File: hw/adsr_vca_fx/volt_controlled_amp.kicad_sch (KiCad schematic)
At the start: 34 parts, among them J9 Conn_01x02, U6 LM13700, U6 TL972

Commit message: updated readme
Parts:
- added J11: Conn_01x02, Connector_PinHeader_2.54mm:PinHeader_1x02_P2.54mm_Vertical, symbol Connector_Generic:Conn_01x02
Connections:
- net GND: now also J11.1 (Pin_1)
- net at R14.2, RV7.1, TP1.1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: now also J11.2 (Pin_2)
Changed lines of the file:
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@@
   (junction (at 204.47 95.25) (diameter 0) (color 0 0 0 0)
   )
+  (junction (at 245.11 149.86) (diameter 0) (color 0 0 0 0)
+  )
   (junction (at 241.3 40.64) (diameter 0) (color 0 0 0 0)
   )
@@
     (stroke (width 0) (type default))
   )
+  (wire (pts (xy 260.35 152.4) (xy 260.35 161.29))
+    (stroke (width 0) (type default))
+  )
   (wire (pts (xy 210.82 53.34) (xy 220.98 53.34))
     (stroke (width 0) (type default))
@@
     (stroke (width 0) (type default))
   )
+  (wire (pts (xy 245.11 149.86) (xy 265.43 149.86))
+    (stroke (width 0) (type default))
+  )
   (wire (pts (xy 158.75 257.81) (xy 158.75 260.35))
     (stroke (width 0) (type default))
@@
   )
   (wire (pts (xy 240.03 97.79) (xy 247.65 97.79))
+    (stroke (width 0) (type default))
+  )
+  (wire (pts (xy 265.43 152.4) (xy 260.35 152.4))
     (stroke (width 0) (type default))
   )
@@
     )
   )
+  (symbol (lib_id "Connector_Generic:Conn_01x02") (at 270.51 152.4 0) (mirror x) (unit 1)
+    (in_bom yes) (on_board yes) (dnp no)
+    (property "Reference" "J11" (at 270.51 147.32 0)
+      (effects (font (size 1.27 1.27)))
+    )
+    (property "Value" "Conn_01x02" (at 270.51 147.32 0)
+      (effects (font (size 1.27 1.27)) hide)
+    )
+    (property "Footprint" "Connector_PinHeader_2.54mm:PinHeader_1x02_P2.54mm_Vertical" (at 270.51 152.4 0)
+      (effects (font (size 1.27 1.27)) hide)
+    )
+    (property "Datasheet" "~" (at 270.51 152.4 0)
+      (effects (font (size 1.27 1.27)) hide)
+    )
+    (pin "1")
+    (pin "2")
+    (instances
+      (project "adsr_vca_fx"
+        (path "/2c7cc946-dcca-4ffb-b6a0-bf0c9ddb491b/00108663-9f1e-44dc-8937-64b7d21ff823"
+          (reference "J11") (unit 1)
+        )
+      )
+    )
+  )
   (symbol (lib_id "Device:R_Potentiometer_Trim") (at 226.06 162.56 270) (unit 1)
     (in_bom yes) (on_board yes) (dnp no)
@@
         )
       )
+    )
+  )
+  (symbol (lib_id "power:GND") (at 260.35 161.29 0) (unit 1)
+    (in_bom yes) (on_board yes) (dnp no) (fields_autoplaced)
+    (property "Reference" "#PWR070" (at 260.35 167.64 0)
+      (effects (font (size 1.27 1.27)) hide)
+    )
+    (property "Value" "GND" (at 260.35 166.37 0)
+      (effects (font (size 1.27 1.27)))
+    )
+    (property "Footprint" "" (at 260.35 161.29 0)
+      (effects (font (size 1.27 1.27)) hide)
+    )
+    (property "Datasheet" "" (at 260.35 161.29 0)
+      (effects (font (size 1.27 1.27)) hide)
+    )
+    (pin "1")
+    (instances
+      (project "adsr_vca_fx"
+        (path "/2c7cc946-dcca-4ffb-b6a0-bf0c9ddb491b/00108663-9f1e-44dc-8937-64b7d21ff823"
+          (reference "#PWR070") (unit 1)
+        )
+      )

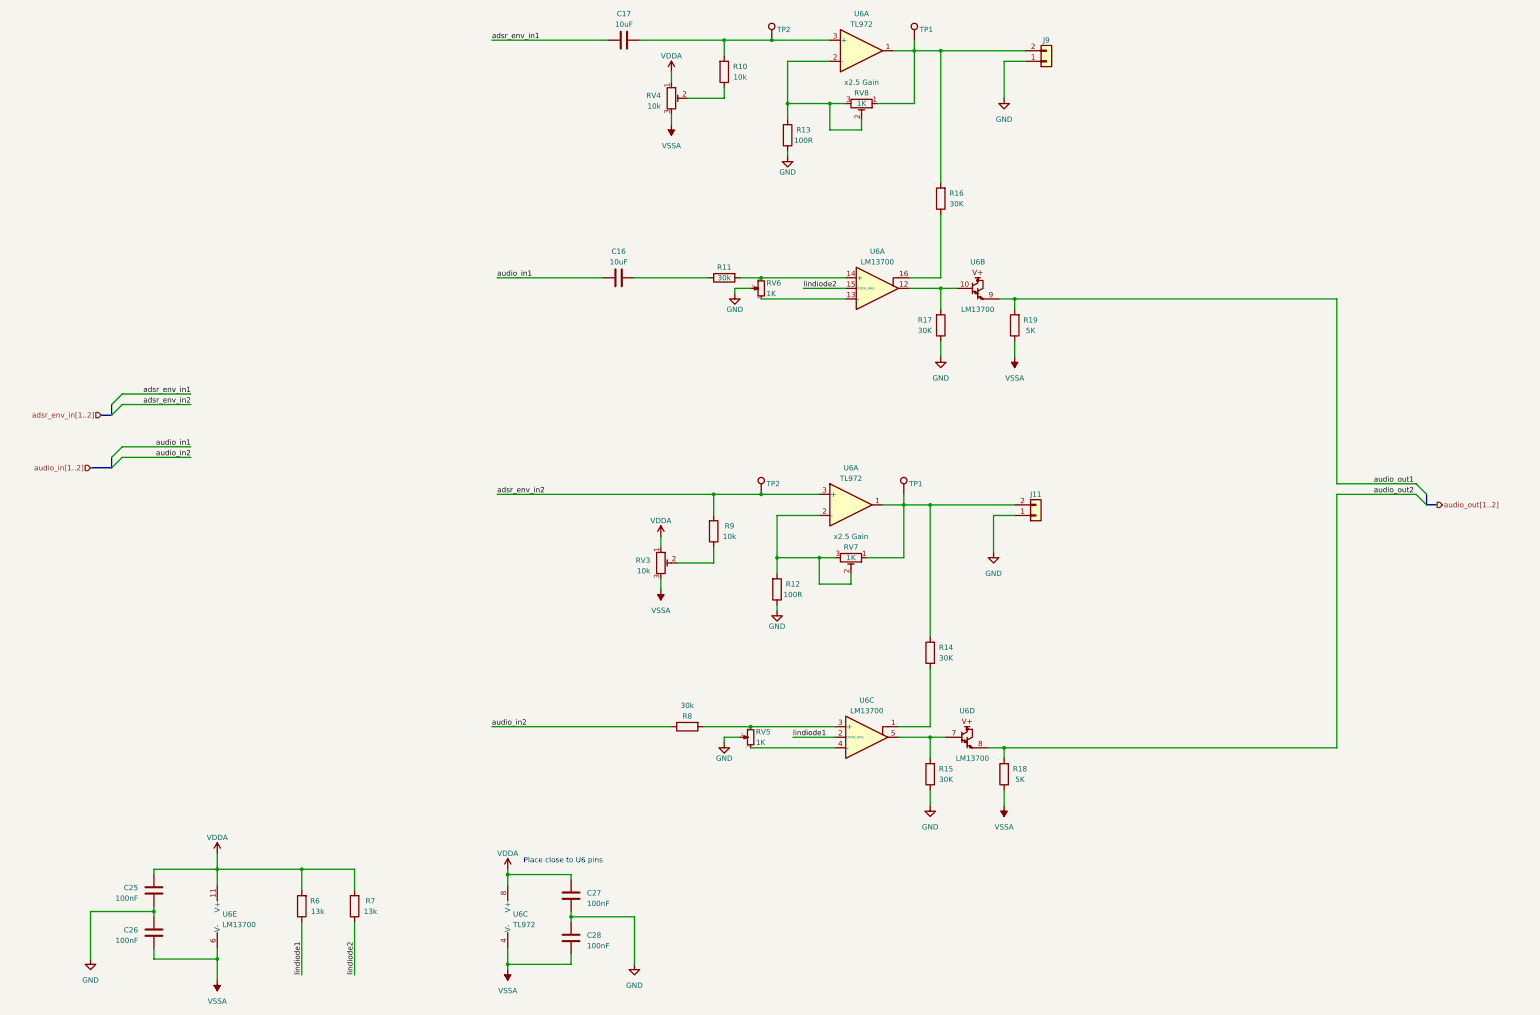
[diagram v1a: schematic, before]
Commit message: modified design into normal/inverted envlope
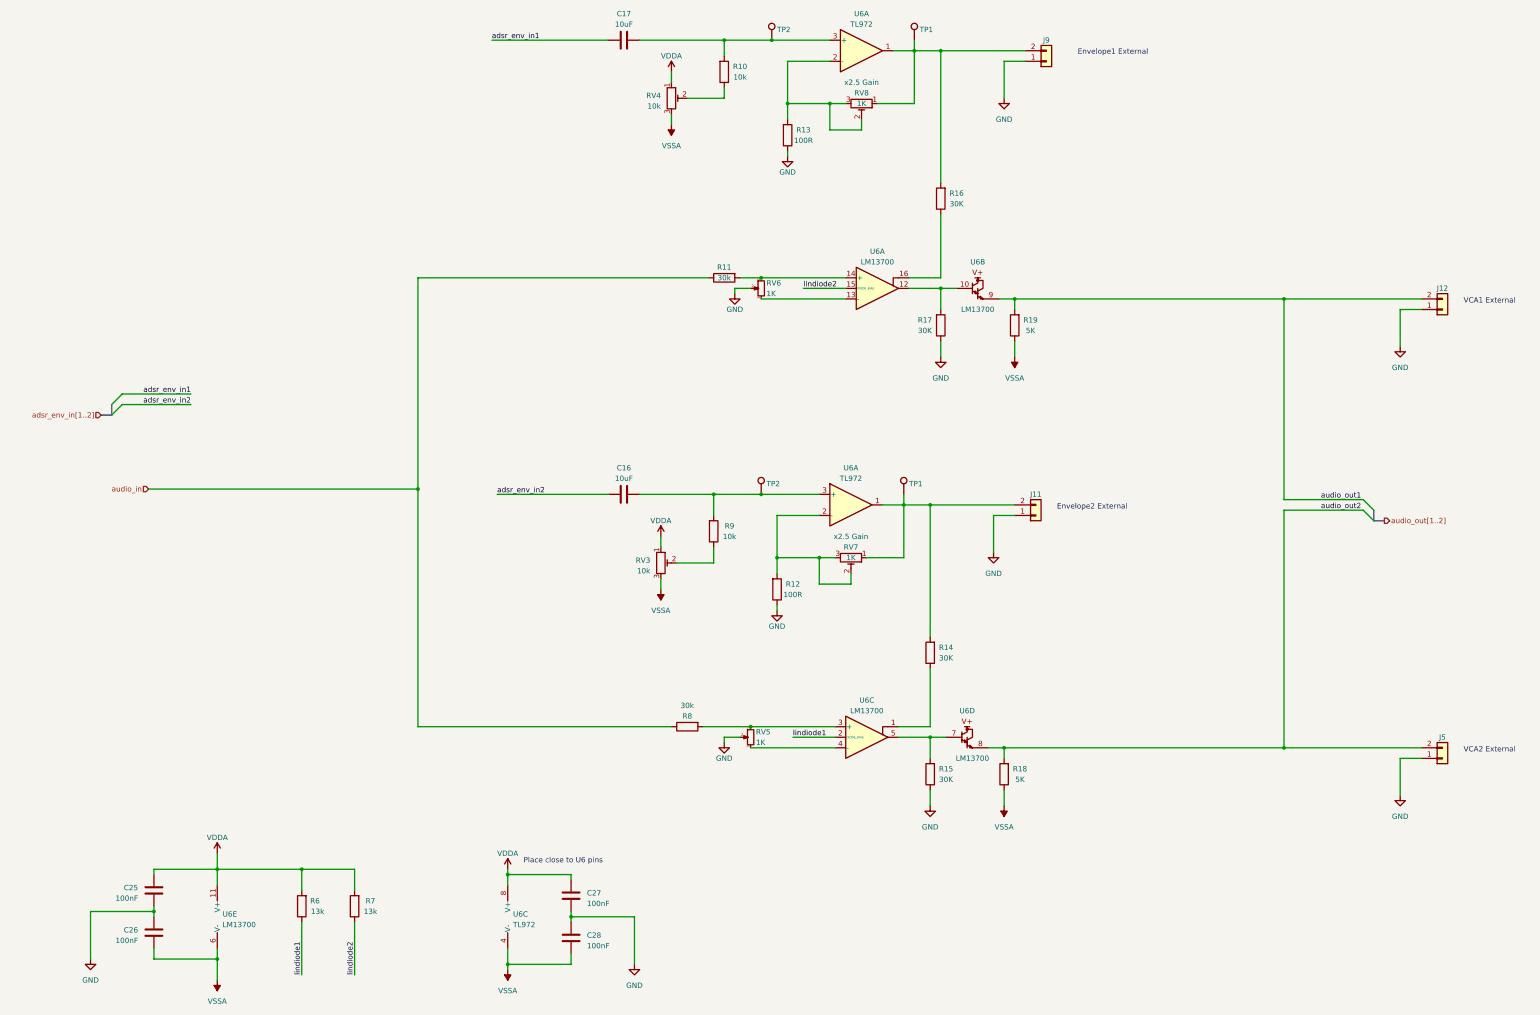
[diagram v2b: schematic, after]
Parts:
- added J12, J5: Conn_01x02, Connector_PinHeader_2.54mm:PinHeader_1x02_P2.54mm_Vertical, symbol Connector_Generic:Conn_01x02
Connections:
- net audio_in1 is gone; now on net adsr_env_in2: C16.1
- net GND: now also J12.1 (Pin_1), J5.1 (Pin_1)
- net adsr_env_in2: no longer R9.2, TP2.1, U6.3 (+)
- net audio_out1: now also J12.2 (Pin_2)
- net audio_out2: now also J5.2 (Pin_2)
- net at C16.2: now also R9.2, TP2.1, U6.3 (+); no longer R11.1
- net audio_in2 renamed audio_in
- net audio_in: now also R11.1
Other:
- note added: "Envelope1 External"
- note added: "Envelope2 External"
- note added: "VCA1 External"
- note added: "VCA2 External"
- moved on the sheet: C16

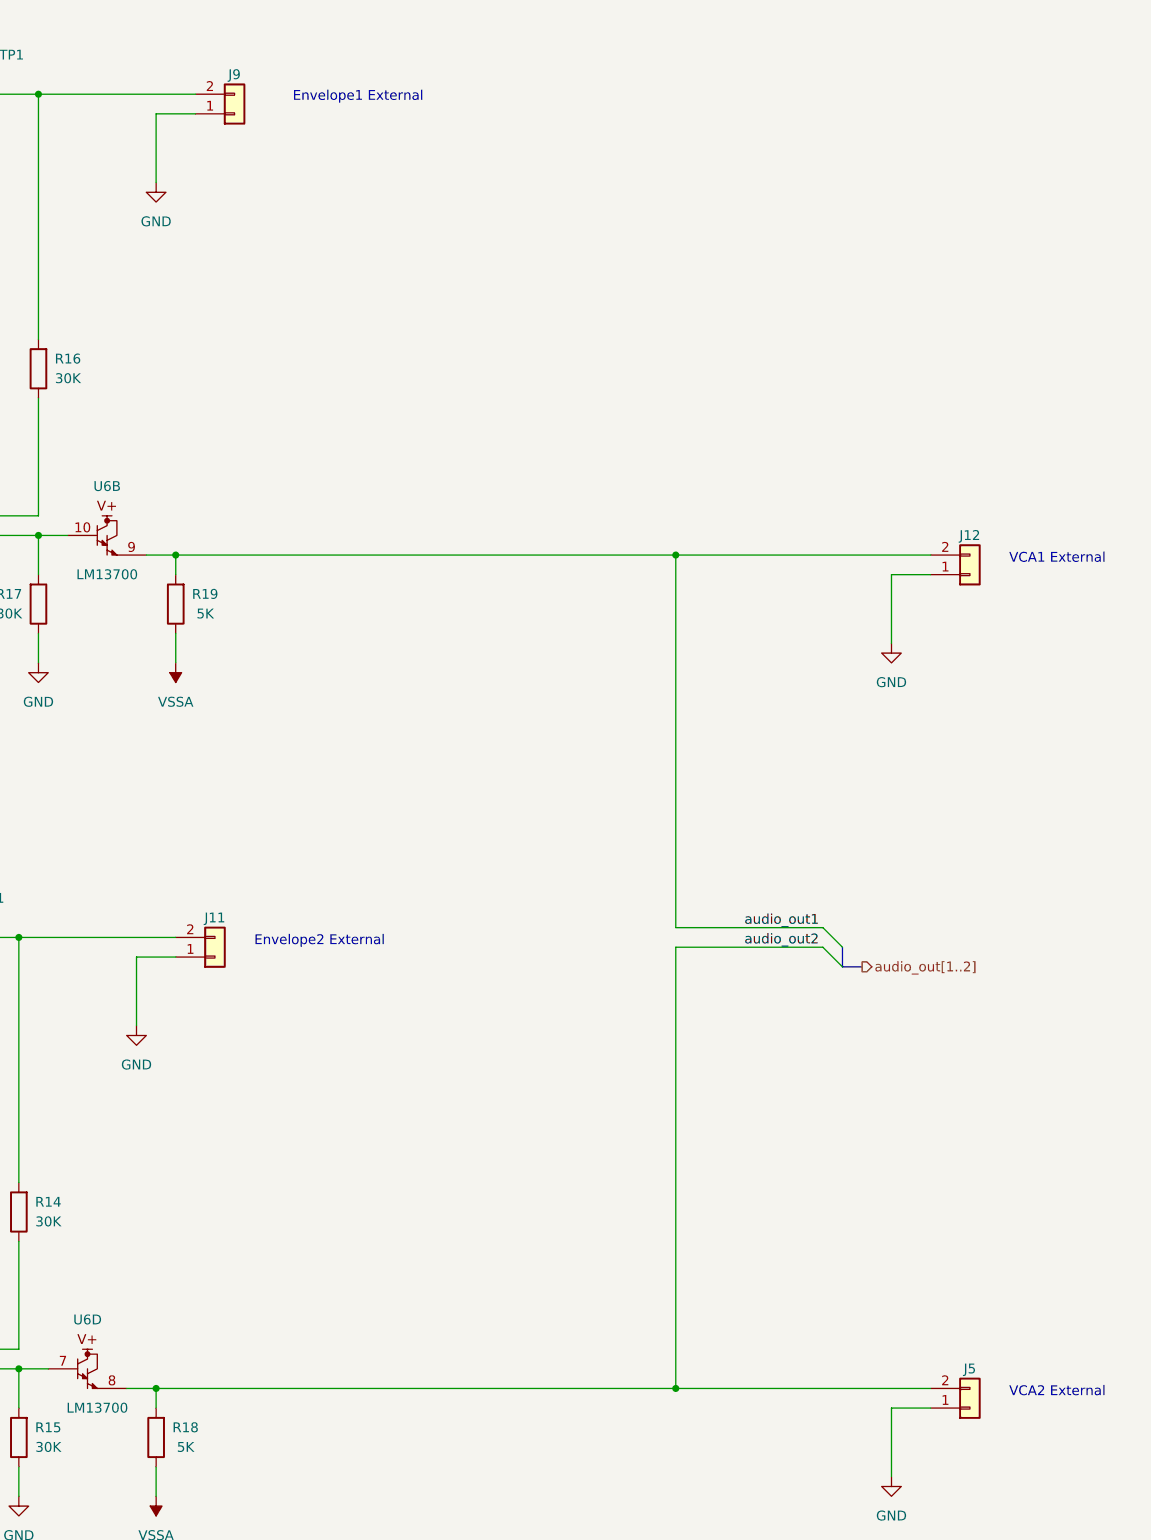
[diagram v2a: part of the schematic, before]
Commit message: updated text labels
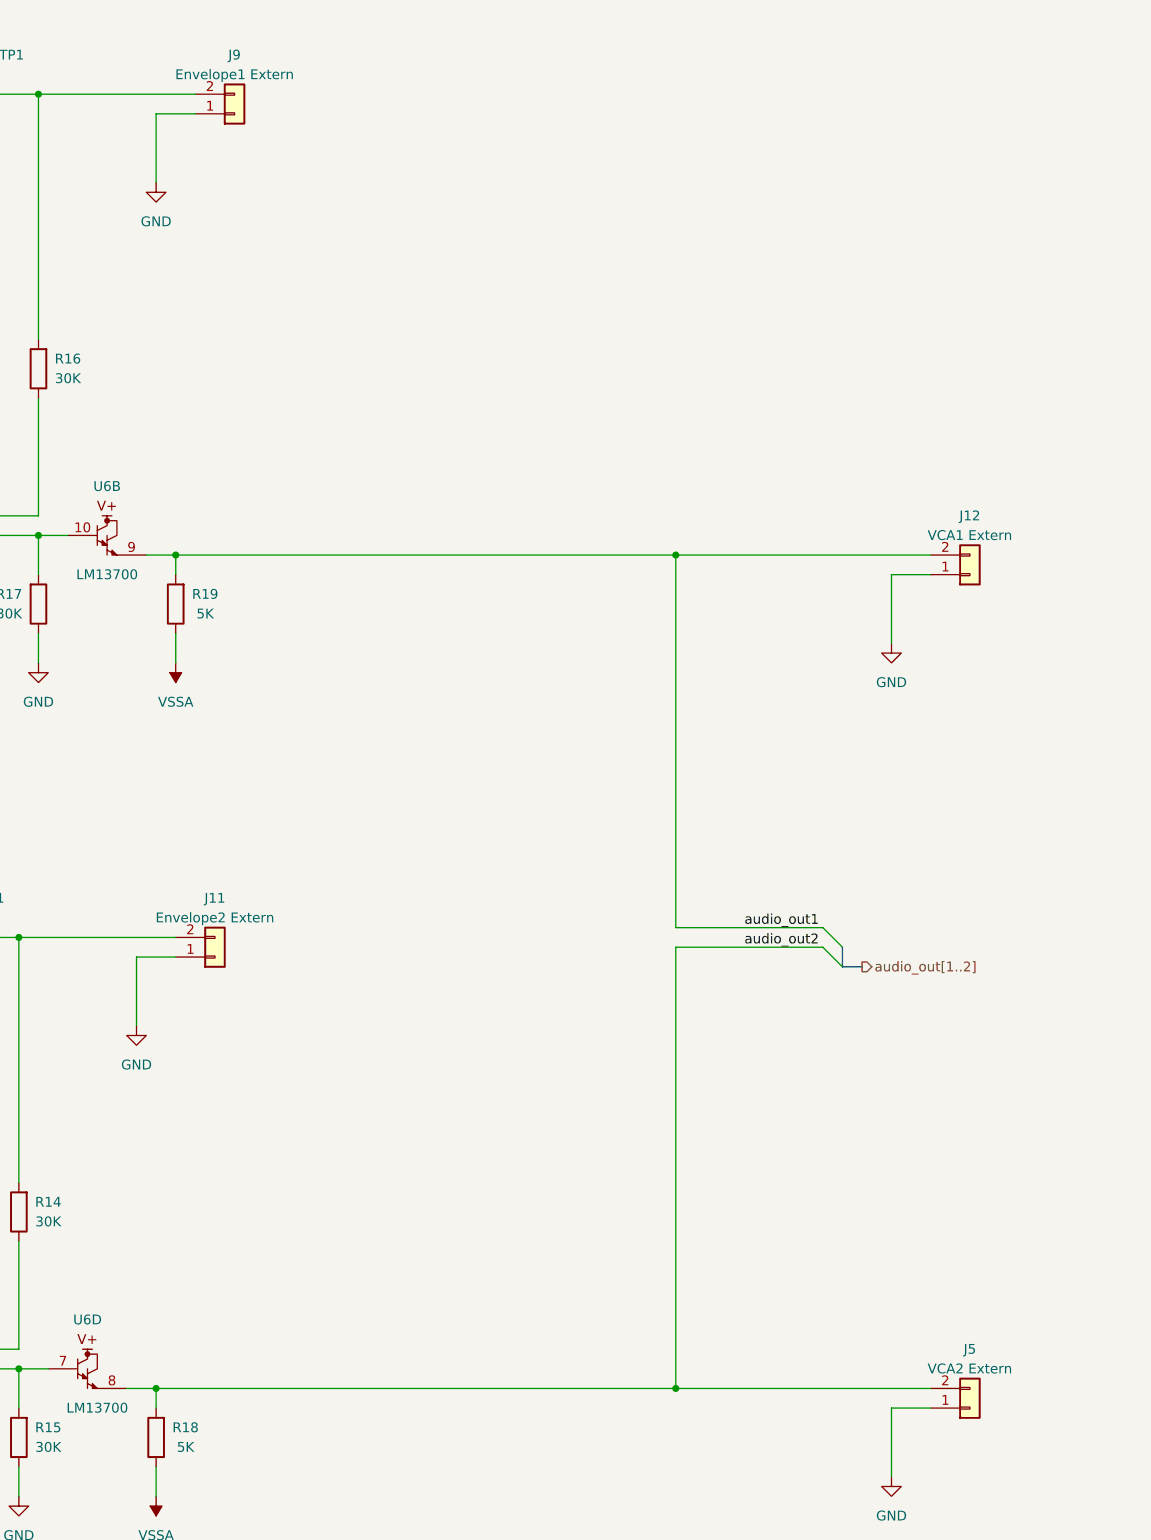
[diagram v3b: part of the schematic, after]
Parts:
- J11: value Conn_01x02 -> Envelope2 Extern
- J12: value Conn_01x02 -> VCA1 Extern
- J5: value Conn_01x02 -> VCA2 Extern
- J9: value Conn_01x02 -> Envelope1 Extern
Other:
- note removed: "Envelope1 External"
- note removed: "Envelope2 External"
- note removed: "VCA1 External"
- note removed: "VCA2 External"
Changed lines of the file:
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@@
-    (effects (font (size 1.27 1.27)) (justify left bottom))
-  )
-  (text "VCA1 External" (at 373.38 101.6 0)
-    (effects (font (size 1.27 1.27)) (justify left bottom))
-  )
-  (text "Envelope1 External" (at 280.5772 41.7704 0)
-    (effects (font (size 1.27 1.27)) (justify left bottom))
-  )
-  (text "VCA2 External" (at 373.38 209.55 0)
-    (effects (font (size 1.27 1.27)) (justify left bottom))
-  )
-  (text "Envelope2 External" (at 275.59 151.13 0)
     (effects (font (size 1.27 1.27)) (justify left bottom))
   )
@@
   (symbol (lib_id "Connector_Generic:Conn_01x02") (at 368.3 102.87 0) (mirror x) (unit 1)
     (in_bom yes) (on_board yes) (dnp no)
-    (property "Reference" "J12" (at 368.3 97.79 0)
-      (effects (font (size 1.27 1.27)))
-    )
-    (property "Value" "Conn_01x02" (at 368.3 97.79 0)
-      (effects (font (size 1.27 1.27)) hide)
+    (property "Reference" "J12" (at 368.3 95.25 0)
+      (effects (font (size 1.27 1.27)))
+    )
+    (property "Value" "VCA1 Extern" (at 368.3 97.79 0)
+      (effects (font (size 1.27 1.27)))
     )
     (property "Footprint" "Connector_PinHeader_2.54mm:PinHeader_1x02_P2.54mm_Vertical" (at 368.3 102.87 0)
@@
   (symbol (lib_id "Connector_Generic:Conn_01x02") (at 270.51 152.4 0) (mirror x) (unit 1)
     (in_bom yes) (on_board yes) (dnp no)
-    (property "Reference" "J11" (at 270.51 147.32 0)
-      (effects (font (size 1.27 1.27)))
-    )
-    (property "Value" "Conn_01x02" (at 270.51 147.32 0)
-      (effects (font (size 1.27 1.27)) hide)
+    (property "Reference" "J11" (at 270.51 144.78 0)
+      (effects (font (size 1.27 1.27)))
+    )
+    (property "Value" "Envelope2 Extern" (at 270.51 147.32 0)
+      (effects (font (size 1.27 1.27)))
     )
     (property "Footprint" "Connector_PinHeader_2.54mm:PinHeader_1x02_P2.54mm_Vertical" (at 270.51 152.4 0)
@@
   (symbol (lib_id "Connector_Generic:Conn_01x02") (at 273.05 43.18 0) (mirror x) (unit 1)
     (in_bom yes) (on_board yes) (dnp no)
-    (property "Reference" "J9" (at 273.05 38.1 0)
-      (effects (font (size 1.27 1.27)))
-    )
-    (property "Value" "Conn_01x02" (at 273.05 38.1 0)
-      (effects (font (size 1.27 1.27)) hide)
+    (property "Reference" "J9" (at 273.05 35.56 0)
+      (effects (font (size 1.27 1.27)))
+    )
+    (property "Value" "Envelope1 Extern" (at 273.05 38.1 0)
+      (effects (font (size 1.27 1.27)))
     )
     (property "Footprint" "Connector_PinHeader_2.54mm:PinHeader_1x02_P2.54mm_Vertical" (at 273.05 43.18 0)
@@
   (symbol (lib_id "Connector_Generic:Conn_01x02") (at 368.3 210.82 0) (mirror x) (unit 1)
     (in_bom yes) (on_board yes) (dnp no)
-    (property "Reference" "J5" (at 368.3 205.74 0)
-      (effects (font (size 1.27 1.27)))
-    )
-    (property "Value" "Conn_01x02" (at 368.3 205.74 0)
-      (effects (font (size 1.27 1.27)) hide)
+    (property "Reference" "J5" (at 368.3 203.2 0)
+      (effects (font (size 1.27 1.27)))
+    )
+    (property "Value" "VCA2 Extern" (at 368.3 205.74 0)
+      (effects (font (size 1.27 1.27)))
     )
     (property "Footprint" "Connector_PinHeader_2.54mm:PinHeader_1x02_P2.54mm_Vertical" (at 368.3 210.82 0)

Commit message: first draft layout
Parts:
- RV10: renamed from RV8; footprint Potentiometer_THT:Potentiometer_Piher_PT-10-V10_Vertical -> Potentiometer_THT:Potentiometer_Runtron_RM-065_Vertical
- RV5: renamed from RV3; footprint Potentiometer_THT:Potentiometer_Piher_PT-10-V10_Vertical -> Potentiometer_THT:Potentiometer_Runtron_RM-065_Vertical
- RV6: renamed from RV4; footprint Potentiometer_THT:Potentiometer_Piher_PT-10-V10_Vertical -> Potentiometer_THT:Potentiometer_Runtron_RM-065_Vertical
- RV7: renamed from RV5; footprint Potentiometer_THT:Potentiometer_Piher_PT-10-V10_Vertical -> Potentiometer_THT:Potentiometer_Runtron_RM-065_Vertical
- RV8: renamed from RV6; footprint Potentiometer_THT:Potentiometer_Piher_PT-10-V10_Vertical -> Potentiometer_THT:Potentiometer_Runtron_RM-065_Vertical
- RV9: renamed from RV7; footprint Potentiometer_THT:Potentiometer_Piher_PT-10-V10_Vertical -> Potentiometer_THT:Potentiometer_Runtron_RM-065_Vertical
- renumbered C17 to C14, C16 to C15, J5 to J10, J11 to J7, J9 to J8, J12 to J9, R9 to R10, R10 to R11, R11 to R12, R12 to R13, R13 to R14, R14 to R15, R15 to R16, R16 to R17, R17 to R18, R18 to R19, R19 to R20, R6 to R7, R7 to R8, R8 to R9, U6 to U4
